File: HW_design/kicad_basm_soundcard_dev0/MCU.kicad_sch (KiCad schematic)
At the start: 31 parts, among them J201 Micro_SD_Card, J202 UART Debug, J203 I2C & SPI Debug, J204 I2S Debug, J205 Power & RGB Debug, Q201 L8050QLT1G, Q202 L8050QLT1G, SW201 SW_MEC_5G, SW202 SW_MEC_5G, U201 ESP32-C3-MINI-1

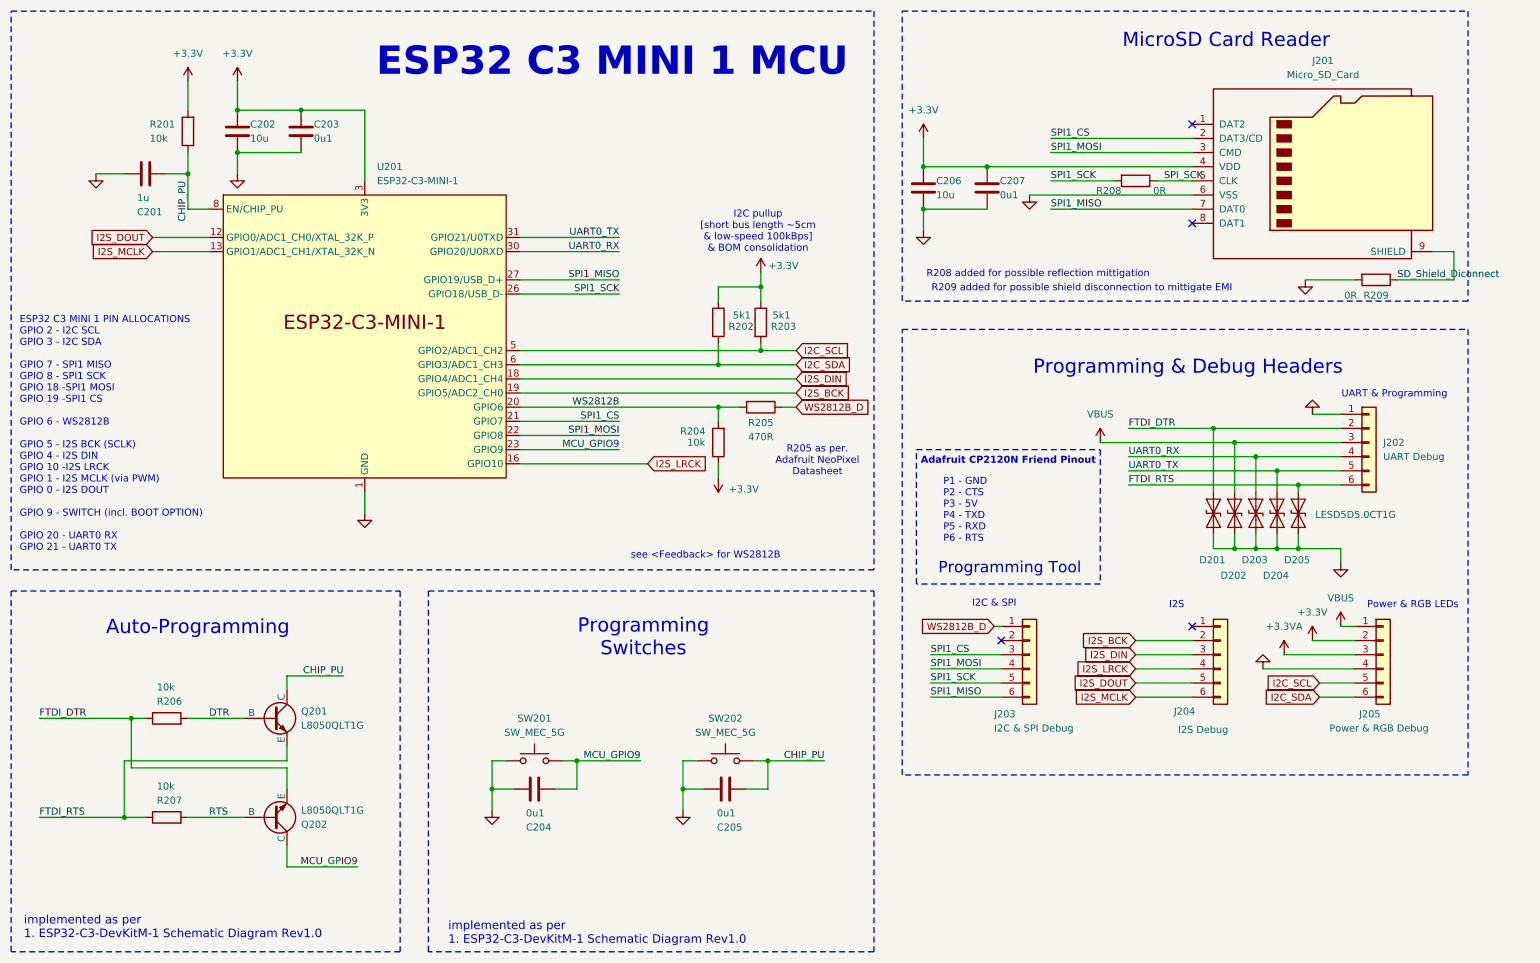
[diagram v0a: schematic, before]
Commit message: Changed Footprints for LED RGB, SD, AudioJack, USB
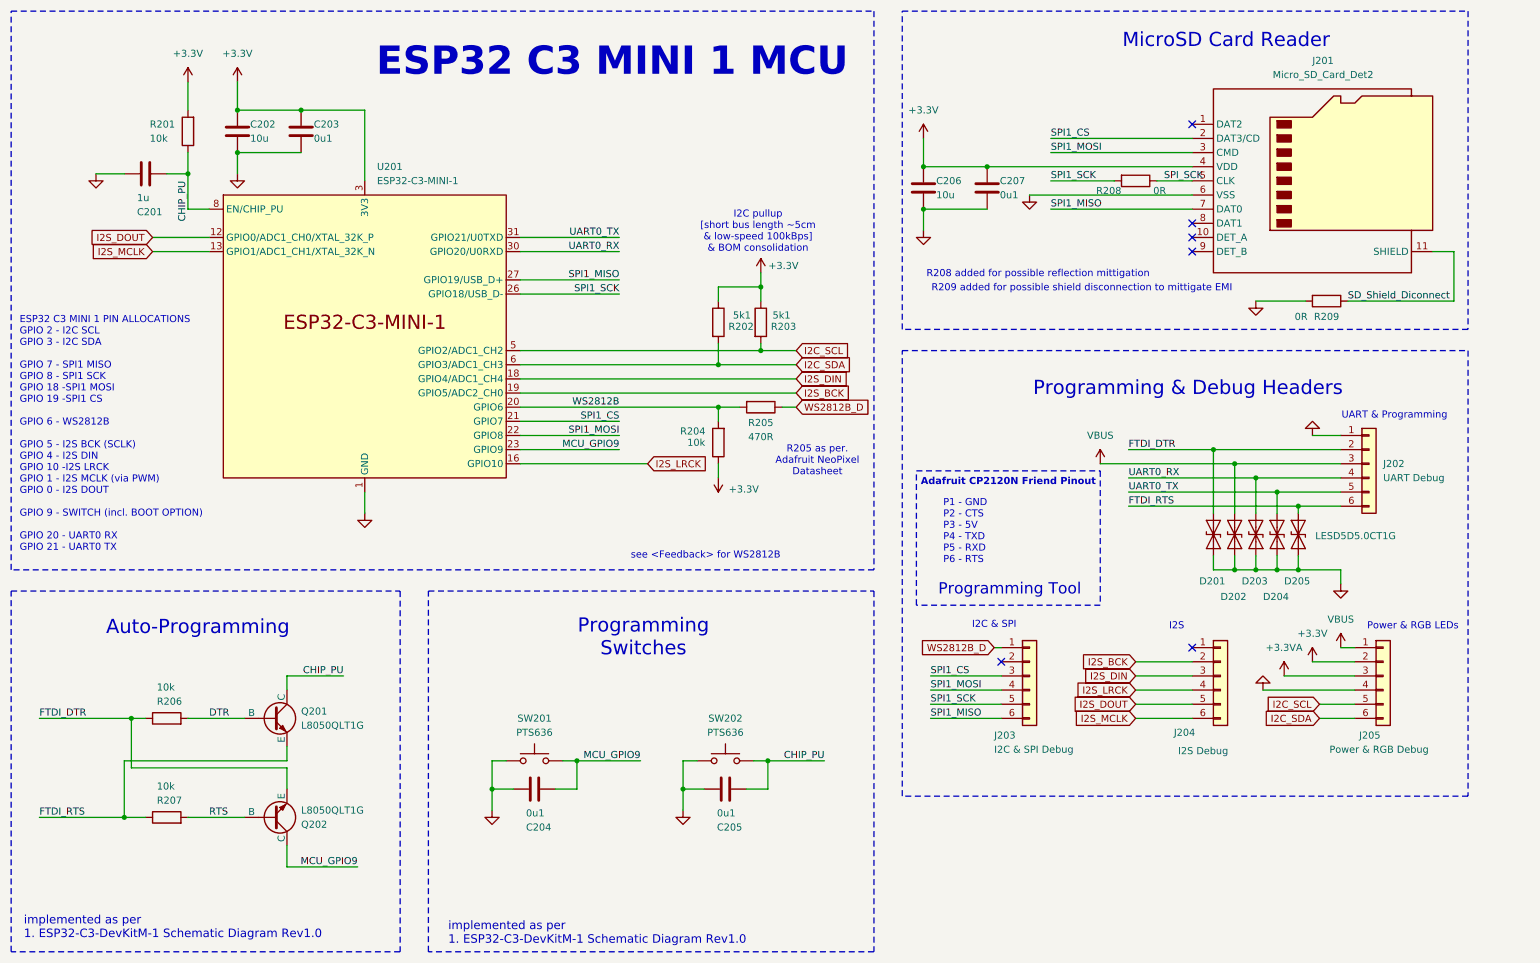
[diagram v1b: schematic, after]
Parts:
- removed J201: Micro_SD_Card, Connector_Card:microSD_HC_Molex_47219-2001, symbol Connector:Micro_SD_Card
- added J201: Micro_SD_Card_Det2, Connector_Card:microSD_HC_Hirose_DM3AT-SF-PEJM5, symbol Connector:Micro_SD_Card_Det2
- C202, C206: footprint Capacitor_SMD:C_0402_1005Metric -> Capacitor_SMD:C_0603_1608Metric
- SW201, SW202: value SW_MEC_5G -> PTS636; footprint (none) -> Button_Switch_SMD:SW_Tactile_SPST_NO_Straight_CK_PTS636Sx25SMTRLFS
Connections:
- net +3.3V: now also J201.4 (VDD)
- net GND: now also J201.6 (VSS)
- net SD_Shield_Diconnect: now also J201.11 (SHIELD)
- net SPI1_CS: now also J201.2 (DAT3/CD)
- net SPI1_MISO: now also J201.7 (DAT0)
- net SPI1_MOSI: now also J201.3 (CMD)
- net SPI_SCK: now also J201.5 (CLK)
- no-connect marks 4 -> 6
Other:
- company: (none) -> BUCHAREST APPLIED STEAM MUSEUM
- title: (none) -> BASM SOUNDCARD
- moved on the sheet: D201, D202, D203, D204, D205, J202, J203, J204, J205, R209
